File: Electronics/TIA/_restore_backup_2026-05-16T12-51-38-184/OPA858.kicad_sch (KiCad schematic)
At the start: 3 parts, among them U1 ${SIM.PARAMS}

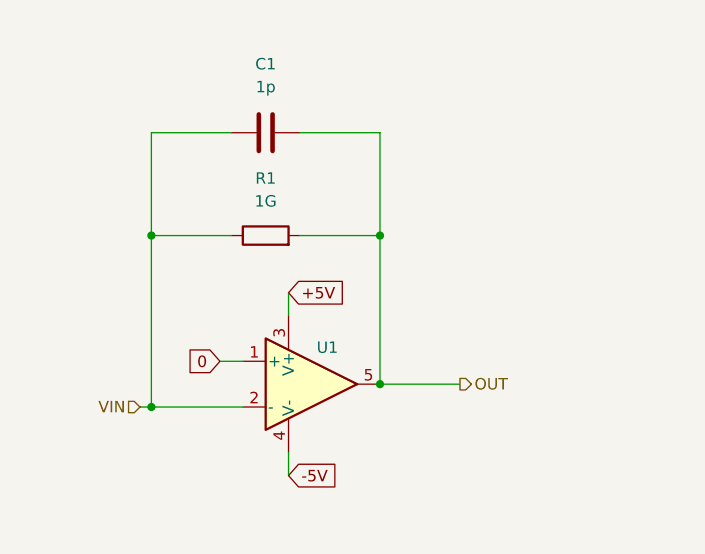
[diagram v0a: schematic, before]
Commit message: Create a robust TIA design following the requirements
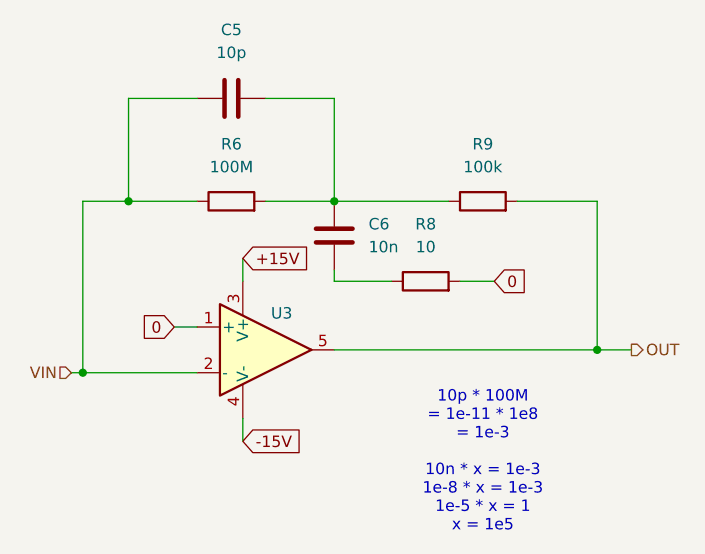
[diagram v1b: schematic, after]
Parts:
- removed C1: 1p, symbol Device:C
- removed R1: 1G, symbol Device:R
- removed U1: ${SIM.PARAMS}, symbol Simulation_SPICE:OPAMP
- added C5: 10p, symbol Device:C
- added C6: 10n, symbol Device:C
- added R6: 100M, symbol Device:R
- added R8: 10, symbol Device:R
- added R9: 100k, symbol Device:R
- added U3: ${SIM.PARAMS}, symbol Simulation_SPICE:OPAMP
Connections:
- net 0: now also R8.2, U3.1 (+)
- net OUT: now also R9.2, U3.5
- net VIN: now also C5.1, R6.1, U3.2 (-)
- new net: C5.2, C6.2, R6.2, R9.1
- new net: C6.1, R8.1
- new net +15V: U3.3 (V+)
- new net -15V: U3.4 (V-)
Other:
- note added: "10p * 100M = 1e-11 * 1e8 = 1e-3 10n * x = 1e-3 1e-8 * x = 1e-3 1e-5 * x = 1 x = 1e5"
